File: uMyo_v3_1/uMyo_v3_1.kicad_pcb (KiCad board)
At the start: 2 copper layers, 47.1 x 28 mm, 53 parts, among them J1 Conn_01x01_Male, J2 Conn_01x01_Male, J4 Conn_01x01_Male, J5 Conn_01x01_Male, J6 Conn_01x02_Female, J7 Conn_01x02_Female, SW1 SW_Push, U1 AD8293G80ARJZ-R2, U2 nRF52810-QFxx, U3 XC6206P332MR_SOT23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

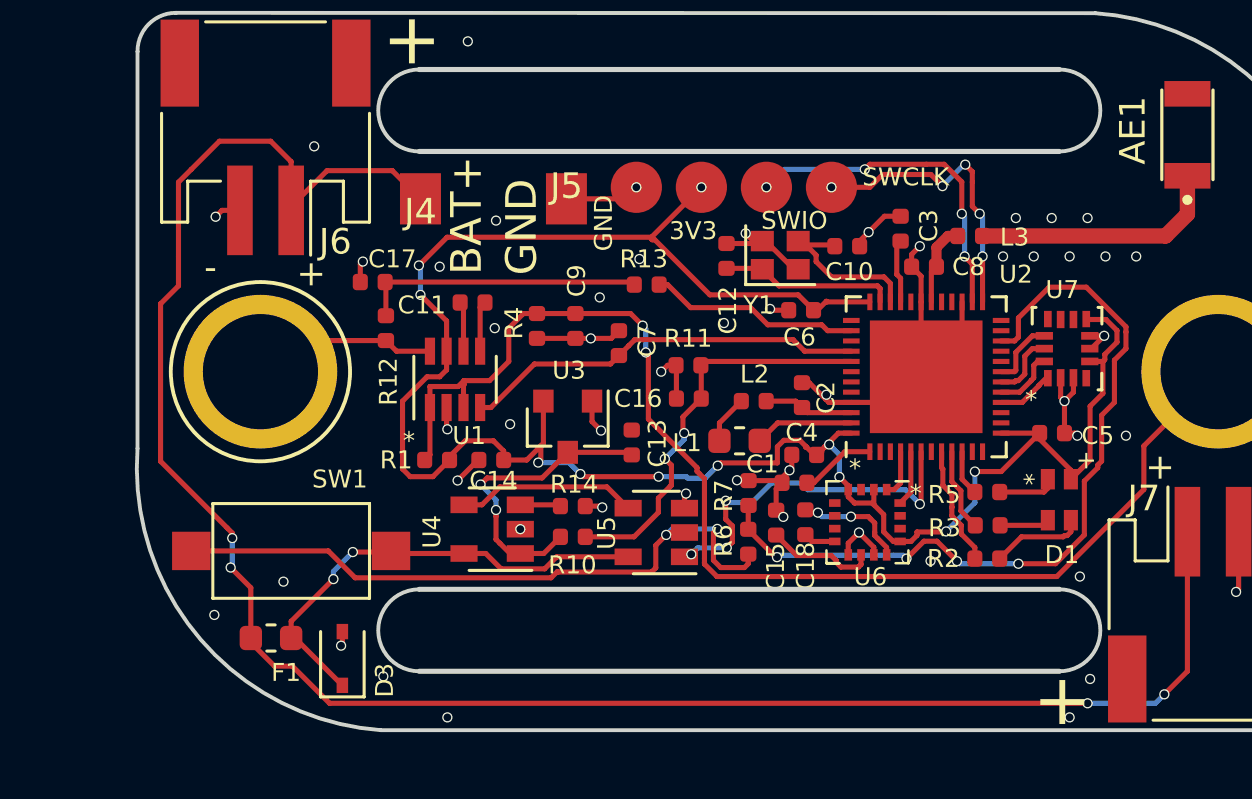
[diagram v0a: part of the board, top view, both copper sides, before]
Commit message: Update to the project to include available and modern parts
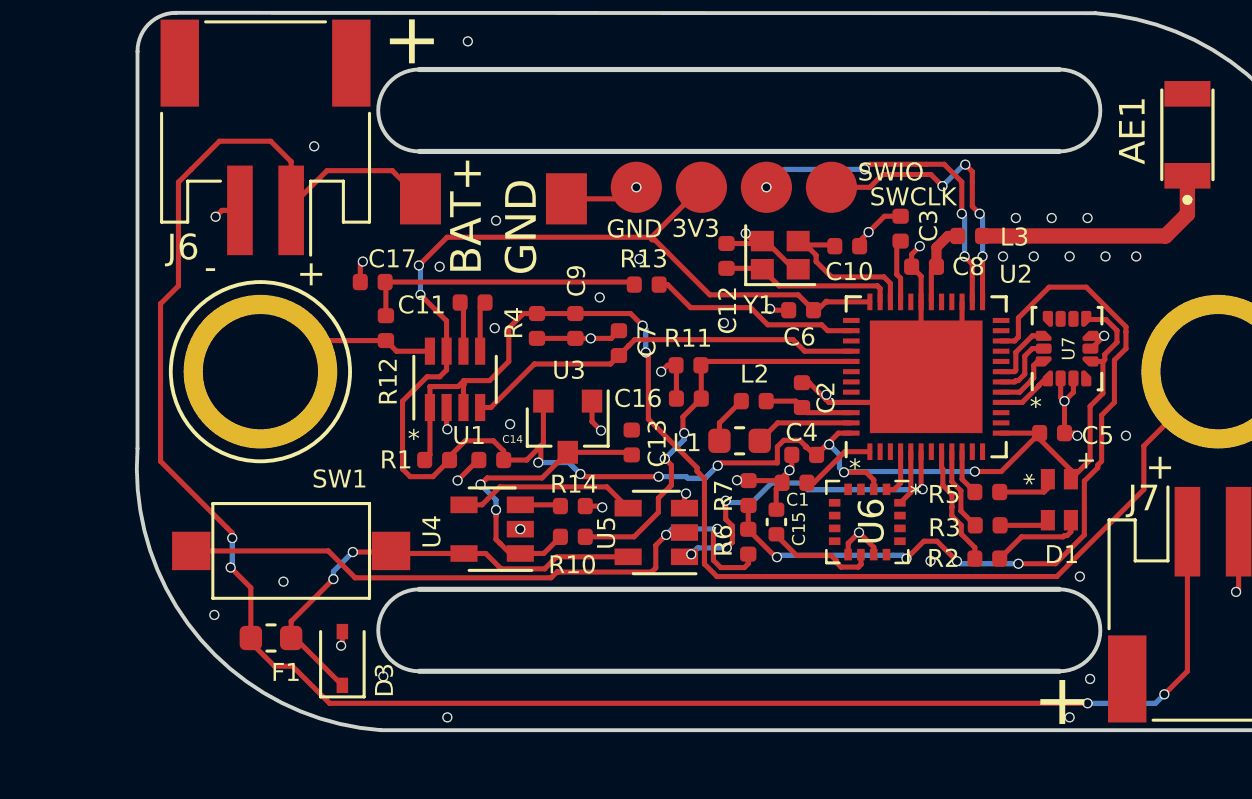
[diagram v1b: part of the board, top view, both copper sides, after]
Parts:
- removed C18: 100 nF, Capacitor_SMD:C_0402_1005Metric
- added G***: LOGO, LOGO, B.Cu at (122.2, 97.6)
- U2: value nRF52810-QFxx -> nRF52832-QFxx
- U6: value QMC5883L -> QMC5883P
- U7: footprint ultimate_library:LGA-14_3x2.5mm_P0.5mm_fix -> Package_LGA:LGA-14_3x2.5mm_P0.5mm_LayoutBorder3x4y
- turned C15 to -90 degrees
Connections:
- C15 pad 1: Net-(C15-Pad1) -> GND
- C15 pad 2: GND -> Net-(C15-Pad2)
- U6 pad 10: Net-(C15-Pad1) -> Net-(C15-Pad2)
- U6 pad 12: Net-(C18-Pad1) -> unconnected-(U6-Pad12)
- U6 pad 13: +3V3 -> unconnected-(U6-Pad13)
- U6 pad 14: (no net) -> unconnected-(U6-Pad14)
- U6 pad 3: (no net) -> unconnected-(U6-Pad3)
- U6 pad 4: +3V3 -> unconnected-(U6-Pad4)
- U6 pad 5: (no net) -> unconnected-(U6-Pad5)
- U6 pad 6: (no net) -> unconnected-(U6-Pad6)
- U6 pad 7: (no net) -> unconnected-(U6-Pad7)
- U6 pad 8: Net-(C18-Pad2) -> unconnected-(U6-Pad8)
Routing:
- net GND: track 50.5 -> 44.8 mm, vias 51 -> 50
- net Net-(C18-Pad1): track 4.36 -> 0.00 mm, vias 2 -> 0
- net Net-(C15-Pad2): track 0.00 -> 4.29 mm
- net Net-(C15-Pad1): track 4.29 -> 0.00 mm
- net +3V3: track 81.9 -> 78.4 mm, vias 11 -> 9
- net Net-(J2-Pad1): track 7.30 -> 5.58 mm
- net Net-(C18-Pad2): track 1.26 -> 0.00 mm
- net SYS_ON: track 14.2 -> 13.2 mm
- net +BATT: track 11.9 -> 11.3 mm
- net SWDCLK: vias 5 -> 4
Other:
- board text added: "MuscleNN V1.0"
- board text removed: "uMyo"
- board text removed: "v3.1"
